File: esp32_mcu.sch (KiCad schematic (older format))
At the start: 2 parts

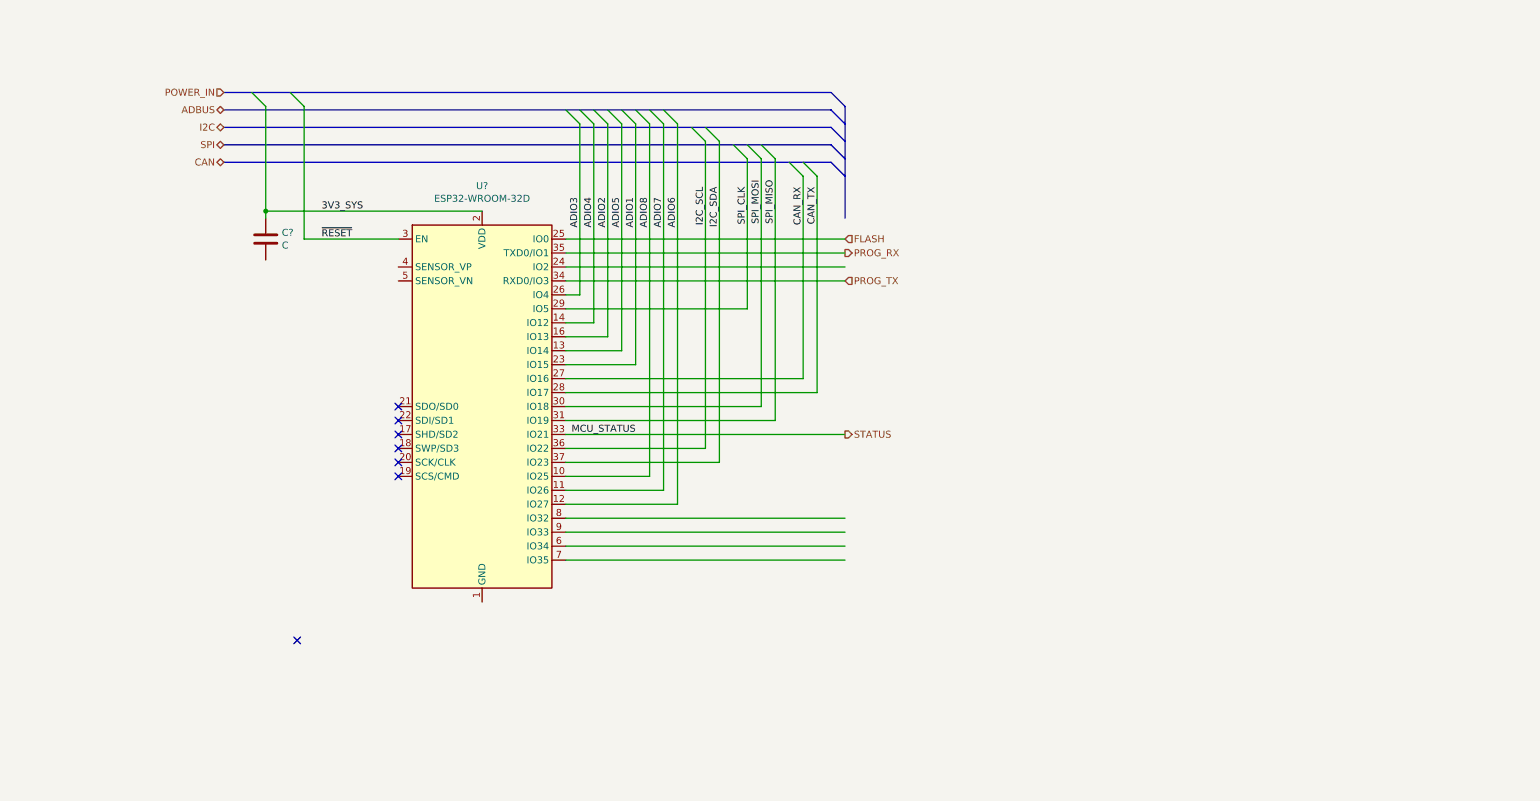
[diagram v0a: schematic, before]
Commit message: Reshuffled MCU connections.
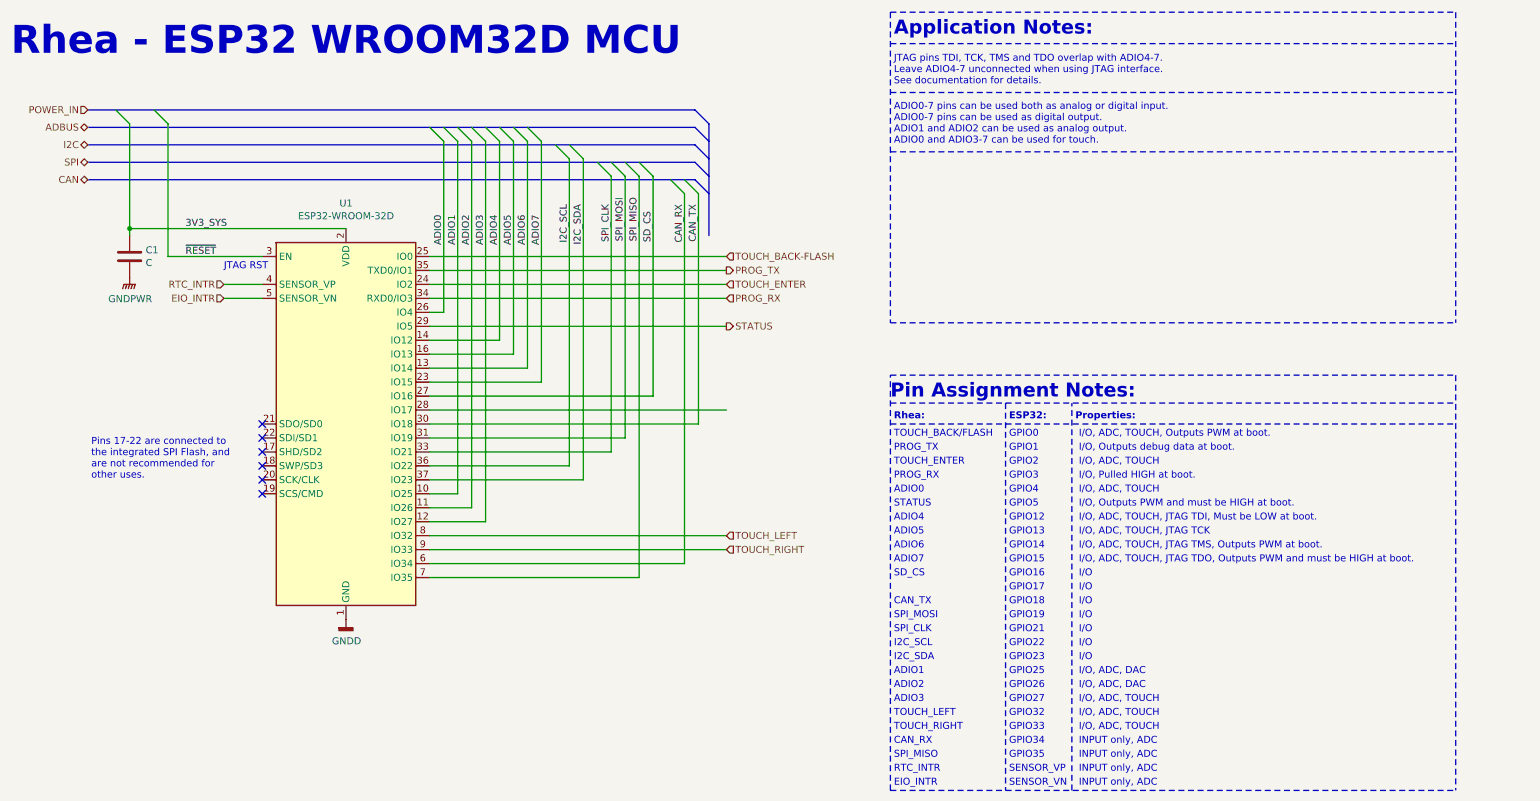
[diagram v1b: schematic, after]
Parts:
- gave numbers to parts that had none: 2
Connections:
- net labels added: ADIO0, EIO_INTR, GNDD, GNDPWR, RTC_INTR, SD_CS, TOUCH_BACK-FLASH, TOUCH_ENTER, TOUCH_LEFT, TOUCH_RIGHT
- net labels removed: ADIO8, FLASH, MCU_STATUS
- wire segments 44 -> 47
- no-connect marks 7 -> 6
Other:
- note added: "ADIO0"
- note added: "ADIO0-7 pins can be used both as analog or digital input.\nADIO0-7 pins can be used as digital output.\nADIO1 and ADIO2 can be used as analog output.\nADIO0 and ADIO3-7 can be used for touch."
- note added: "ADIO1"
- note added: "ADIO2"
- note added: "ADIO3"
- note added: "ADIO4"
- note added: "ADIO5"
- note added: "ADIO6"
- note added: "ADIO7"
- note added: "Application Notes:"
- note added: "CAN_RX"
- note added: "CAN_TX"
- note added: "EIO_INTR"
- note added: "ESP32:"
- note added: "GPIO0"
- note added: "GPIO1"
- note added: "GPIO12"
- note added: "GPIO13"
- note added: "GPIO14"
- note added: "GPIO15"
- note added: "GPIO16"
- note added: "GPIO17"
- note added: "GPIO18"
- note added: "GPIO19"
- note added: "GPIO2"
- note added: "GPIO21"
- note added: "GPIO22"
- note added: "GPIO23"
- note added: "GPIO25"
- note added: "GPIO26"
- note added: "GPIO27"
- note added: "GPIO3"
- note added: "GPIO32"
- note added: "GPIO33"
- note added: "GPIO34"
- note added: "GPIO35"
- note added: "GPIO4"
- note added: "GPIO5"
- note added: "I/O"
- note added: "I/O, ADC, DAC"
- note added: "I/O, ADC, TOUCH"
- note added: "I/O, ADC, TOUCH, JTAG TCK"
- note added: "I/O, ADC, TOUCH, JTAG TDI, Must be LOW at boot."
- note added: "I/O, ADC, TOUCH, JTAG TDO, Outputs PWM and must be HIGH at boot."
- note added: "I/O, ADC, TOUCH, JTAG TMS, Outputs PWM at boot."
- note added: "I/O, ADC, TOUCH, Outputs PWM at boot."
- note added: "I/O, Outputs PWM and must be HIGH at boot."
- note added: "I/O, Outputs debug data at boot."
- note added: "I/O, Pulled HIGH at boot."
- note added: "I2C_SCL"
- note added: "I2C_SDA"
- note added: "INPUT only, ADC"
- note added: "JTAG RST"
- note added: "JTAG pins TDI, TCK, TMS and TDO overlap with ADIO4-7.\nLeave ADIO4-7 unconnected when using JTAG interface. \nSee documentation for details."
- note added: "PROG_RX"
- note added: "PROG_TX"
- note added: "Pin Assignment Notes:"
- note added: "Pins 17-22 are connected to \nthe integrated SPI Flash, and \nare not recommended for \nother uses."
- note added: "Properties:"
- note added: "RTC_INTR"
- note added: "Rhea - ESP32 WROOM32D MCU"
- note added: "Rhea:"
- note added: "SD_CS"
- note added: "SENSOR_VN"
- note added: "SENSOR_VP"
- note added: "SPI_CLK"
- note added: "SPI_MISO"
- note added: "SPI_MOSI"
- note added: "STATUS"
- note added: "TOUCH_BACK/FLASH"
- note added: "TOUCH_ENTER"
- note added: "TOUCH_LEFT"
- note added: "TOUCH_RIGHT"
- moved on the sheet: C1, U1

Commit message: External headers early draft.
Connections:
- net ~POWER_ALERT: now reaches U1.28 (IO17)
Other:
- note added: "~POWER_ALERT"
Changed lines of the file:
@@
 Wire Bus Line
 	1225 1500 5575 1500
+Text HLabel 5800 3525 2    50   Input ~ 0
+~POWER_ALERT
+Text Notes 7000 4825 0    50   ~ 0
+~POWER_ALERT
 $EndSCHEMATC

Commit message: Power regulation updates.
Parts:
- renumbered C1 to C8, U1 to U12
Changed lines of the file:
@@
 $EndDescr
 $Comp
-L RF_Module:ESP32-WROOM-32D U1
+L RF_Module:ESP32-WROOM-32D U12
 U 1 1 5E2DCA0A
 P 3075 3625
-F 0 "U1" H 3075 5206 50  0000 C CNN
+F 0 "U12" H 3075 5206 50  0000 C CNN
 F 1 "ESP32-WROOM-32D" H 3075 5115 50  0000 C CNN
 F 2 "RF_Module:ESP32-WROOM-32" H 3075 2125 50  0001 C CNN
@@
 NoConn ~ 2475 4125
 $Comp
-L Device:C C1
+L Device:C C8
 U 1 1 5E313C40
 P 1525 2425
-F 0 "C1" H 1640 2471 50  0000 L CNN
+F 0 "C8" H 1640 2471 50  0000 L CNN
 F 1 "C" H 1640 2380 50  0000 L CNN
 F 2 "" H 1563 2275 50  0001 C CNN
@@
 Pins 17-22 are connected to \nthe integrated SPI Flash, and \nare not recommended for \nother uses.
 $Comp
-L power:GNDPWR #PWR0119
+L power:GNDPWR #PWR035
 U 1 1 5E2FCB5C
 P 1525 2575
-F 0 "#PWR0119" H 1525 2375 50  0001 C CNN
+F 0 "#PWR035" H 1525 2375 50  0001 C CNN
 F 1 "GNDPWR" H 1529 2421 50  0000 C CNN
 F 2 "" H 1525 2525 50  0001 C CNN
@@
 $EndComp
 $Comp
-L power:GNDD #PWR0120
+L power:GNDD #PWR036
 U 1 1 5E2FD35C
 P 3075 5025
-F 0 "#PWR0120" H 3075 4775 50  0001 C CNN
+F 0 "#PWR036" H 3075 4775 50  0001 C CNN
 F 1 "GNDD" H 3079 4870 50  0000 C CNN
 F 2 "" H 3075 5025 50  0001 C CNN
@@
 Text Notes 675  1000 0    200  ~ 40
 Rhea - ESP32 WROOM32D MCU
-Wire Bus Line
-	1225 1625 5575 1625
-Wire Bus Line
-	1225 1375 5575 1375
-Wire Bus Line
-	1225 1875 5575 1875
-Wire Bus Line
-	1225 1750 5575 1750
-Wire Bus Line
-	5675 1475 5675 2275
-Wire Bus Line
-	1225 1500 5575 1500
 Text HLabel 5800 3525 2    50   Input ~ 0
 ~POWER_ALERT
 Text Notes 7000 4825 0    50   ~ 0
 ~POWER_ALERT
+Wire Bus Line
+	1225 1625 5575 1625
+Wire Bus Line
+	1225 1375 5575 1375
+Wire Bus Line
+	1225 1875 5575 1875
+Wire Bus Line
+	1225 1750 5575 1750
+Wire Bus Line
+	5675 1475 5675 2275
+Wire Bus Line
+	1225 1500 5575 1500
 $EndSCHEMATC
